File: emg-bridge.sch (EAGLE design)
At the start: 27 parts, among them J1 RJ25_4X1, J2 RJ25_4X1, J3 M03_0.156IN-RA, J4 POWER_JACKPTH, J5 USB-B, J6 M05X2RAF, U1 DC_ISOLATOR-RKZ0505D

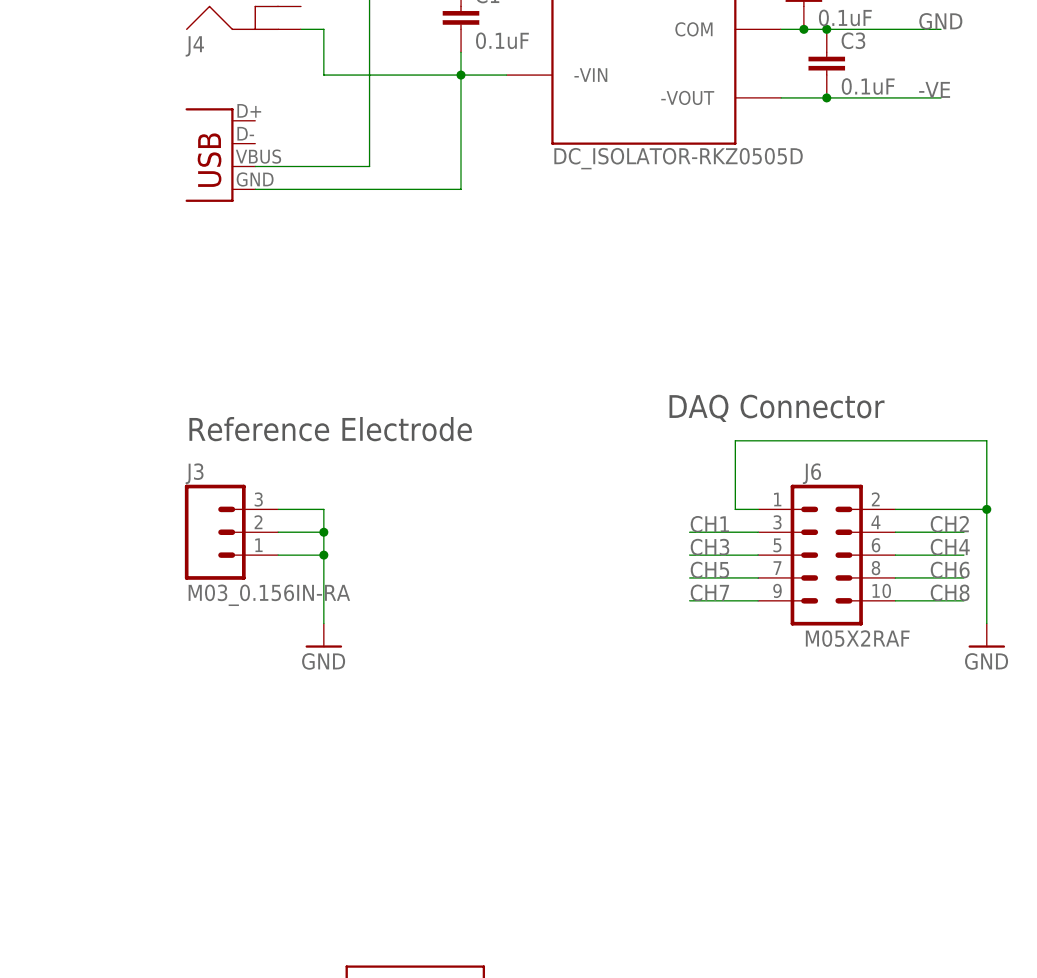
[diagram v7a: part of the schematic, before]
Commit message: Added LED.
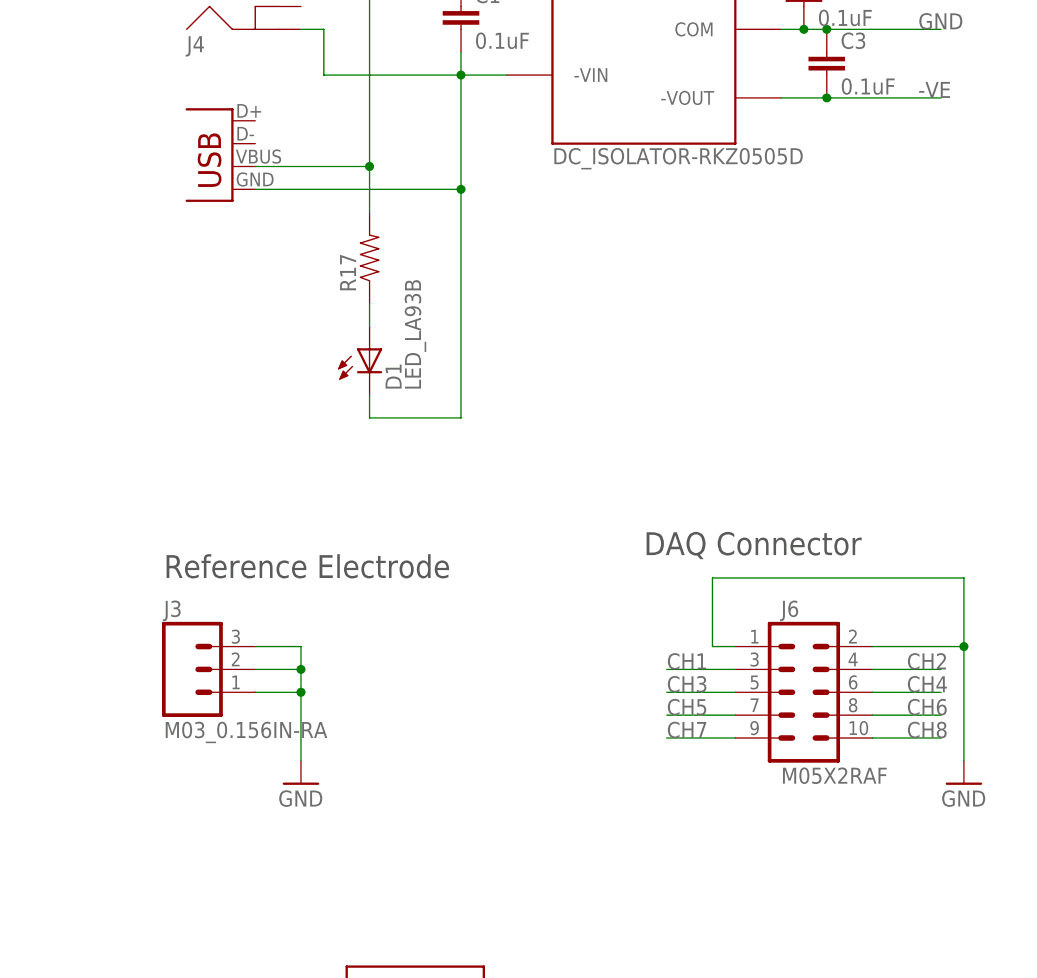
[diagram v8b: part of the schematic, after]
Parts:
- added D1: LED_LA93B, eagle-lib:LED_LA93B
- added R17: (no value), SparkFun-Passives:RESISTOR0805-RES
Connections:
- new net N$4: D1.A, R17.1
- net DGND: now also D1.C
- net N$2: now also R17.2
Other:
- moved on the sheet: J3, J6
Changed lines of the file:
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@@
 <part name="C3" library="SparkFun-Capacitors" deviceset="CAP" device="0805" value="0.1uF"/>
 <part name="J4" library="SparkFun-Connectors" deviceset="POWER_JACK" device="PTH"/>
+<part name="D1" library="eagle-lib" deviceset="LED" device="_LA93B"/>
+<part name="R17" library="SparkFun-Passives" deviceset="RESISTOR" device="0805-RES"/>
 </parts>
 <sheets>
@@
 <text x="30.48" y="175.26" size="2.54" layer="97">Amplifier Connectors</text>
 <text x="154.94" y="165.1" size="2.54" layer="97">Power Conversion</text>
-<text x="208.28" y="104.14" size="2.54" layer="97">DAQ Connector</text>
-<text x="154.94" y="101.6" size="2.54" layer="97">Reference Electrode</text>
+<text x="205.74" y="88.9" size="2.54" layer="97">DAQ Connector</text>
+<text x="152.4" y="86.36" size="2.54" layer="97">Reference Electrode</text>
 </plain>
 <instances>
@@
 <instance part="GND10" gate="1" x="93.98" y="121.92"/>
 <instance part="GND11" gate="1" x="93.98" y="147.32"/>
-<instance part="GND12" gate="1" x="170.18" y="78.74"/>
-<instance part="GND13" gate="1" x="243.84" y="78.74"/>
-<instance part="J3" gate="G$1" x="157.48" y="91.44"/>
-<instance part="J6" gate="G$1" x="226.06" y="88.9"/>
+<instance part="GND12" gate="1" x="167.64" y="63.5"/>
+<instance part="GND13" gate="1" x="241.3" y="63.5"/>
+<instance part="J3" gate="G$1" x="154.94" y="76.2"/>
+<instance part="J6" gate="G$1" x="223.52" y="73.66"/>
 <instance part="FRAME1" gate="G$1" x="0" y="0"/>
 <instance part="FRAME1" gate="G$2" x="172.72" y="0"/>
@@
 <instance part="C3" gate="G$1" x="226.06" y="142.24"/>
 <instance part="J4" gate="G$1" x="165.1" y="144.78"/>
+<instance part="D1" gate="G$1" x="175.26" y="109.22"/>
+<instance part="R17" gate="G$1" x="175.26" y="121.92" rot="R90"/>
 </instances>
 <busses>
@@
 <net name="GND" class="0">
 <segment>
-<wire x1="233.68" y1="93.98" x2="243.84" y2="93.98" width="0.1524" layer="91"/>
+<wire x1="231.14" y1="78.74" x2="241.3" y2="78.74" width="0.1524" layer="91"/>
 <pinref part="GND13" gate="1" pin="GND"/>
-<wire x1="243.84" y1="81.28" x2="243.84" y2="93.98" width="0.1524" layer="91"/>
+<wire x1="241.3" y1="66.04" x2="241.3" y2="78.74" width="0.1524" layer="91"/>
 <pinref part="J6" gate="G$1" pin="2"/>
 <pinref part="J6" gate="G$1" pin="1"/>
-<wire x1="218.44" y1="93.98" x2="215.9" y2="93.98" width="0.1524" layer="91"/>
-<wire x1="215.9" y1="93.98" x2="215.9" y2="101.6" width="0.1524" layer="91"/>
-<wire x1="215.9" y1="101.6" x2="243.84" y2="101.6" width="0.1524" layer="91"/>
-<wire x1="243.84" y1="101.6" x2="243.84" y2="93.98" width="0.1524" layer="91"/>
-<junction x="243.84" y="93.98"/>
-</segment>
-<segment>
-<wire x1="165.1" y1="91.44" x2="170.18" y2="91.44" width="0.1524" layer="91"/>
+<wire x1="215.9" y1="78.74" x2="213.36" y2="78.74" width="0.1524" layer="91"/>
+<wire x1="213.36" y1="78.74" x2="213.36" y2="86.36" width="0.1524" layer="91"/>
+<wire x1="213.36" y1="86.36" x2="241.3" y2="86.36" width="0.1524" layer="91"/>
+<wire x1="241.3" y1="86.36" x2="241.3" y2="78.74" width="0.1524" layer="91"/>
+<junction x="241.3" y="78.74"/>
+</segment>
+<segment>
+<wire x1="162.56" y1="76.2" x2="167.64" y2="76.2" width="0.1524" layer="91"/>
 <pinref part="GND12" gate="1" pin="GND"/>
-<wire x1="170.18" y1="81.28" x2="170.18" y2="88.9" width="0.1524" layer="91"/>
+<wire x1="167.64" y1="66.04" x2="167.64" y2="73.66" width="0.1524" layer="91"/>
 <pinref part="J3" gate="G$1" pin="2"/>
 <pinref part="J3" gate="G$1" pin="3"/>
-<wire x1="170.18" y1="88.9" x2="170.18" y2="91.44" width="0.1524" layer="91"/>
-<wire x1="165.1" y1="93.98" x2="170.18" y2="93.98" width="0.1524" layer="91"/>
-<wire x1="170.18" y1="93.98" x2="170.18" y2="91.44" width="0.1524" layer="91"/>
-<junction x="170.18" y="91.44"/>
+<wire x1="167.64" y1="73.66" x2="167.64" y2="76.2" width="0.1524" layer="91"/>
+<wire x1="162.56" y1="78.74" x2="167.64" y2="78.74" width="0.1524" layer="91"/>
+<wire x1="167.64" y1="78.74" x2="167.64" y2="76.2" width="0.1524" layer="91"/>
+<junction x="167.64" y="76.2"/>
 <pinref part="J3" gate="G$1" pin="1"/>
-<wire x1="165.1" y1="88.9" x2="170.18" y2="88.9" width="0.1524" layer="91"/>
-<junction x="170.18" y="88.9"/>
+<wire x1="162.56" y1="73.66" x2="167.64" y2="73.66" width="0.1524" layer="91"/>
+<junction x="167.64" y="73.66"/>
 </segment>
 <segment>
@@
 <net name="CH1" class="0">
 <segment>
-<wire x1="218.44" y1="91.44" x2="210.82" y2="91.44" width="0.1524" layer="91"/>
-<label x="210.82" y="91.44" size="1.778" layer="95"/>
+<wire x1="215.9" y1="76.2" x2="208.28" y2="76.2" width="0.1524" layer="91"/>
+<label x="208.28" y="76.2" size="1.778" layer="95"/>
 <pinref part="J6" gate="G$1" pin="3"/>
 </segment>
@@
 <net name="CH3" class="0">
 <segment>
-<wire x1="218.44" y1="88.9" x2="210.82" y2="88.9" width="0.1524" layer="91"/>
-<label x="210.82" y="88.9" size="1.778" layer="95"/>
+<wire x1="215.9" y1="73.66" x2="208.28" y2="73.66" width="0.1524" layer="91"/>
+<label x="208.28" y="73.66" size="1.778" layer="95"/>
 <pinref part="J6" gate="G$1" pin="5"/>
 </segment>
@@
 <net name="CH5" class="0">
 <segment>
-<wire x1="218.44" y1="86.36" x2="210.82" y2="86.36" width="0.1524" layer="91"/>
-<label x="210.82" y="86.36" size="1.778" layer="95"/>
+<wire x1="215.9" y1="71.12" x2="208.28" y2="71.12" width="0.1524" layer="91"/>
+<label x="208.28" y="71.12" size="1.778" layer="95"/>
 <pinref part="J6" gate="G$1" pin="7"/>
 </segment>
@@
 <net name="CH7" class="0">
 <segment>
-<wire x1="218.44" y1="83.82" x2="210.82" y2="83.82" width="0.1524" layer="91"/>
-<label x="210.82" y="83.82" size="1.778" layer="95"/>
+<wire x1="215.9" y1="68.58" x2="208.28" y2="68.58" width="0.1524" layer="91"/>
+<label x="208.28" y="68.58" size="1.778" layer="95"/>
 <pinref part="J6" gate="G$1" pin="9"/>
 </segment>
@@
 <net name="CH2" class="0">
 <segment>
-<wire x1="233.68" y1="91.44" x2="241.3" y2="91.44" width="0.1524" layer="91"/>
-<label x="237.49" y="91.44" size="1.778" layer="95"/>
+<wire x1="231.14" y1="76.2" x2="238.76" y2="76.2" width="0.1524" layer="91"/>
+<label x="234.95" y="76.2" size="1.778" layer="95"/>
 <pinref part="J6" gate="G$1" pin="4"/>
 </segment>
@@
 <net name="CH4" class="0">
 <segment>
-<wire x1="233.68" y1="88.9" x2="241.3" y2="88.9" width="0.1524" layer="91"/>
-<label x="237.49" y="88.9" size="1.778" layer="95"/>
+<wire x1="231.14" y1="73.66" x2="238.76" y2="73.66" width="0.1524" layer="91"/>
+<label x="234.95" y="73.66" size="1.778" layer="95"/>
 <pinref part="J6" gate="G$1" pin="6"/>
 </segment>
@@
 <net name="CH6" class="0">
 <segment>
-<wire x1="233.68" y1="86.36" x2="241.3" y2="86.36" width="0.1524" layer="91"/>
-<label x="237.49" y="86.36" size="1.778" layer="95"/>
+<wire x1="231.14" y1="71.12" x2="238.76" y2="71.12" width="0.1524" layer="91"/>
+<label x="234.95" y="71.12" size="1.778" layer="95"/>
 <pinref part="J6" gate="G$1" pin="8"/>
 </segment>
@@
 <net name="CH8" class="0">
 <segment>
-<wire x1="233.68" y1="83.82" x2="241.3" y2="83.82" width="0.1524" layer="91"/>
-<label x="237.49" y="83.82" size="1.778" layer="95"/>
+<wire x1="231.14" y1="68.58" x2="238.76" y2="68.58" width="0.1524" layer="91"/>
+<label x="234.95" y="68.58" size="1.778" layer="95"/>
 <pinref part="J6" gate="G$1" pin="10"/>
 </segment>
@@
 <wire x1="162.56" y1="129.54" x2="185.42" y2="129.54" width="0.1524" layer="91"/>
 <wire x1="185.42" y1="129.54" x2="185.42" y2="142.24" width="0.1524" layer="91"/>
+<wire x1="185.42" y1="129.54" x2="185.42" y2="104.14" width="0.1524" layer="91"/>
+<junction x="185.42" y="129.54"/>
+<pinref part="D1" gate="G$1" pin="C"/>
+<wire x1="185.42" y1="104.14" x2="175.26" y2="104.14" width="0.1524" layer="91"/>
+<wire x1="175.26" y1="104.14" x2="175.26" y2="106.68" width="0.1524" layer="91"/>
 </segment>
 </net>
@@
 <wire x1="175.26" y1="132.08" x2="175.26" y2="152.4" width="0.1524" layer="91"/>
 <junction x="175.26" y="152.4"/>
-</segment>
-</net>
+<pinref part="R17" gate="G$1" pin="2"/>
+<wire x1="175.26" y1="127" x2="175.26" y2="132.08" width="0.1524" layer="91"/>
+<junction x="175.26" y="132.08"/>
+</segment>
+</net>
+<net name="N$4" class="0">
+<segment>
+<pinref part="R17" gate="G$1" pin="1"/>
+<pinref part="D1" gate="G$1" pin="A"/>
+<wire x1="175.26" y1="116.84" x2="175.26" y2="114.3" width="0.1524" layer="91"/>
+</segment>
+</net>
